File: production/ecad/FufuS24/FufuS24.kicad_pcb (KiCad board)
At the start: 4 copper layers, 120 x 120 mm, 137 parts, among them J1 Conn_01x02, J10 691137710002, J11 USB_B_Micro, J12 691137710002, J13 5033950410, J2 Conn_01x02, J3 691137710002, J5 691137710004, J6 5025840270, J7 691137710002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

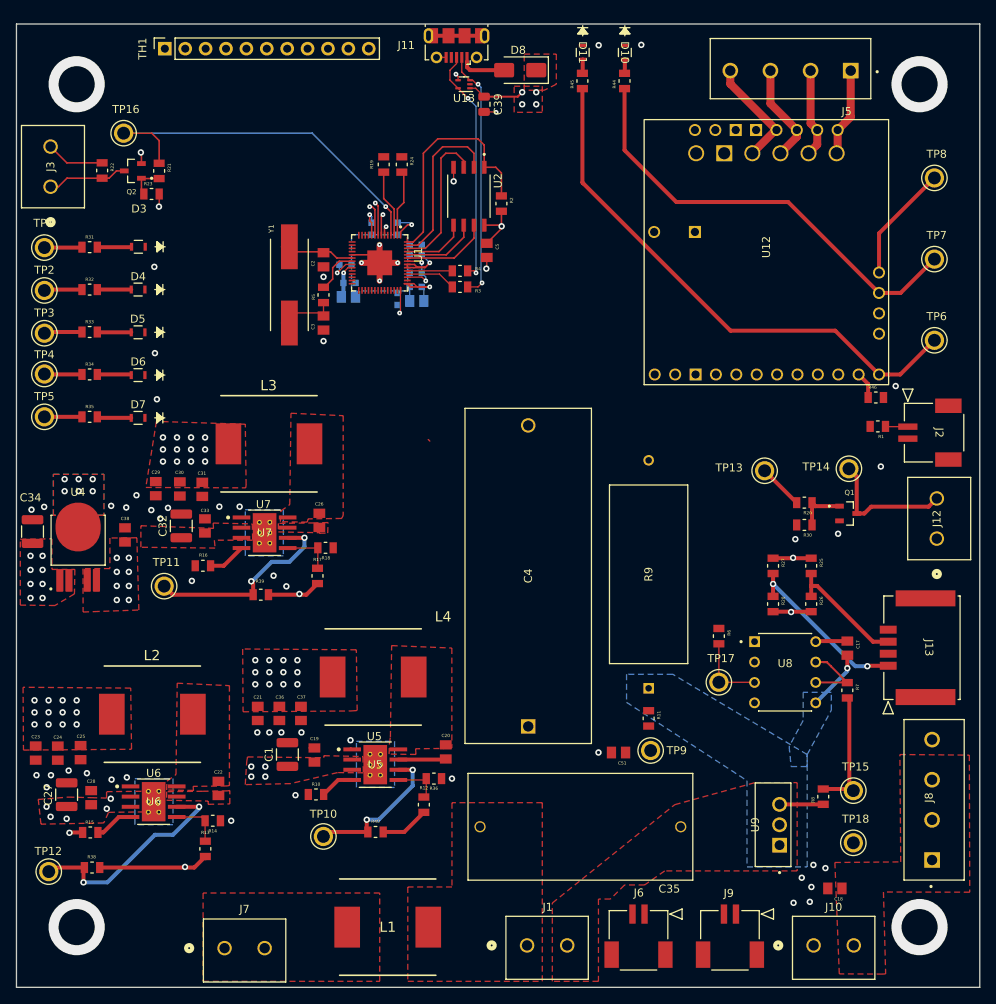
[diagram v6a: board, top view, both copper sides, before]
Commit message: major layout changes
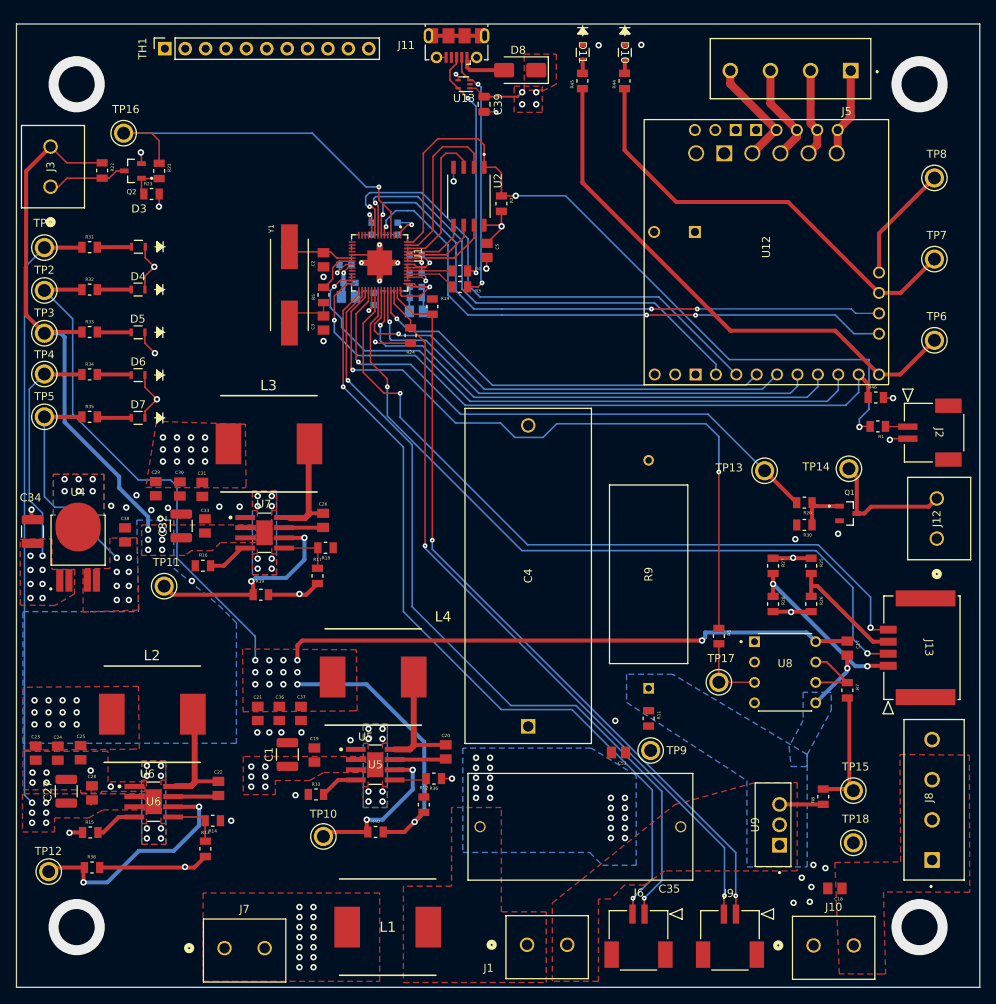
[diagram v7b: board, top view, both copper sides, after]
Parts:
- U5, U6, U7: footprint footprints:DDA0008E-MFG -> footprints:DDA0008E-IPC_A
- moved R24 21.3 mm to (129.1, 68.8), turned to 90 degrees
- moved R19 18.7 mm to (131.8, 65.2)
- moved C13 8.54 mm to (124.5, 64.2), turned to 90 degrees
- moved C9 2.27 mm to (129.8, 64.1), turned to 180 degrees
- moved C10 1.30 mm to (129.8, 65.8)
- moved C28 0.60 mm to (89.4, 125.8)
- moved C26 0.47 mm to (118.2, 91.8)
- moved C27 0.43 mm to (86.2, 125.6)
- moved J1 0.08 mm to (143.6, 144.7)
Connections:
- R35 pad 1: +3V3 -> +3.3V
- TP5 pad TP: +3V3 -> +3.3V
- U1 pad 2: SDA_EXT -> unconnected-(U1-GPIO0-Pad2)
- U1 pad 3: SCL_EXT -> unconnected-(U1-GPIO1-Pad3)
- U1 pad 40: unconnected-(U1-GPIO28_ADC2-Pad40) -> SDA_EXT
- U1 pad 41: unconnected-(U1-GPIO29_ADC3-Pad41) -> SCL_EXT
- U12 pad 15: MOSI1 -> Motor_SPI1_RX
- U12 pad 16: MISO1 -> Motor_SPI1_TX
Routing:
- net +16V: track 15.1 -> 170.6 mm, vias 12 -> 14
- net HOT_LED_POS: track 0.00 -> 100.6 mm, vias 0 -> 2
- net HOT_LED_NEG: track 0.00 -> 100.4 mm, vias 0 -> 2
- net Watersense1_Read: track 0.00 -> 95.3 mm, vias 0 -> 2
- net Watersense2_Read: track 0.00 -> 93.5 mm, vias 0 -> 2
- net SCL_EXT: track 8.40 -> 96.5 mm, vias 0 -> 2
- net SDA_EXT: track 8.29 -> 94.8 mm, vias 0 -> 2
- net Heat_PWM1: track 0.00 -> 85.1 mm, vias 0 -> 2
- net Motor_RST: track 3.36 -> 82.7 mm, vias 0 -> 1
- net Motor_SLP: track 0.00 -> 76.6 mm, vias 0 -> 1
- net Motor_BIN1: track 1.15 -> 73.9 mm, vias 1 -> 3
- net Motor_BIN2: track 2.65 -> 75.0 mm, vias 1 -> 3
- net +48V: track 4.80 -> 75.4 mm, vias 9 -> 26
- net Motor_SPI1_CSn: track 0.00 -> 66.0 mm, vias 0 -> 1
- net Pump_Enable: track 5.64 -> 71.5 mm, vias 0 -> 1
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- added copper zone on B.Cu, net +12V
- added copper zone on In1.Cu, net +3.3V
- added copper zone on In1.Cu, net +48V
- added copper zone on B.Cu, net +5V
- added copper zone on In1.Cu, net +5V
- removed copper zone on F.Cu, net Net-(U5-SW)
- removed copper zone on F.Cu, net Net-(U6-BOOT)
- removed copper zone on F.Cu, net Net-(U6-SW)
- removed copper zone on F.Cu, net Net-(U7-BOOT)
- removed copper zone on F.Cu, net Net-(U7-SW)
